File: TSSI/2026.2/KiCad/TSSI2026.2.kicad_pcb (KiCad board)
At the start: 2 copper layers, 66 x 35 mm, 32 parts, among them J1 Conn_01x02, J2 Conn_01x02, J3 Conn_02x02, Q1 IRLZ34N, T555 Test555, U1 LM555xN, U2 IRLZ34N, U3 IRLZ34N, U4 4001, U5 4069

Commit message: Add files via upload
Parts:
- moved U5 0.27 mm to (72.3, 24.5)

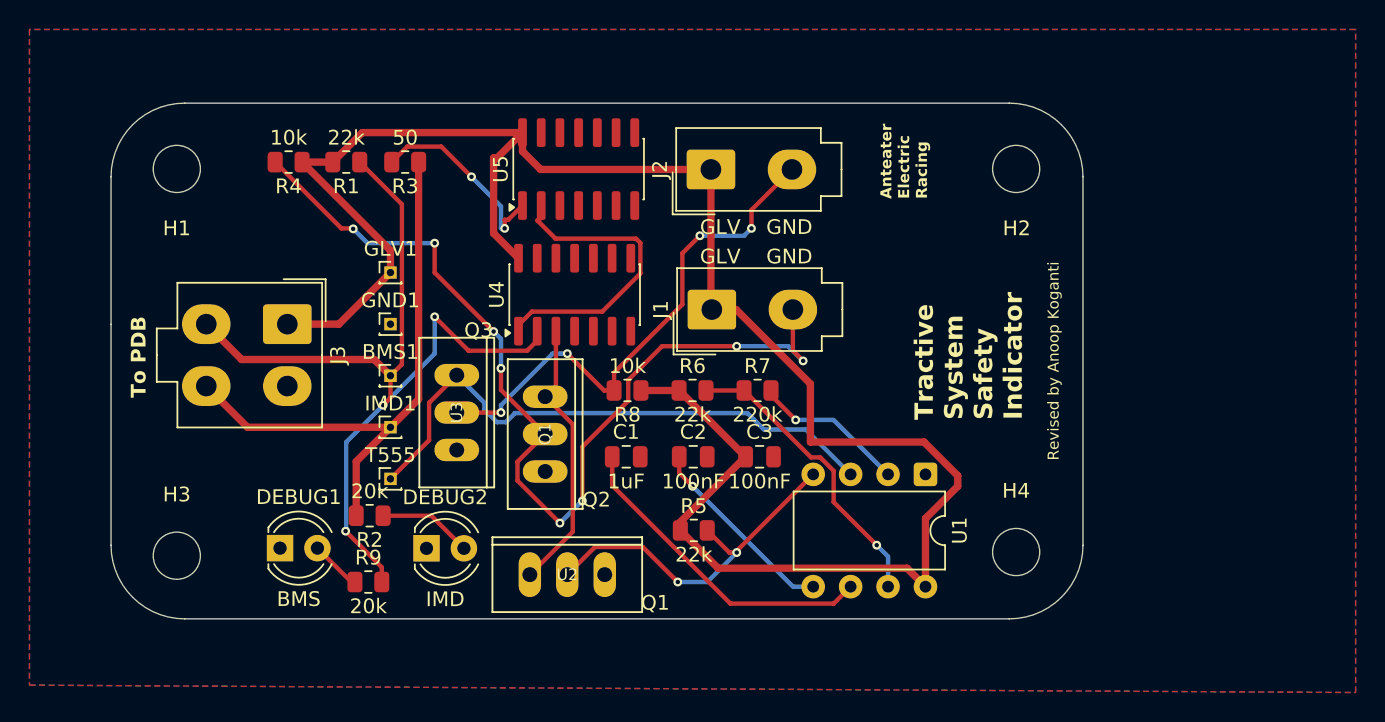
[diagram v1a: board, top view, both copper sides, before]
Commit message: Add silkscreen connectors
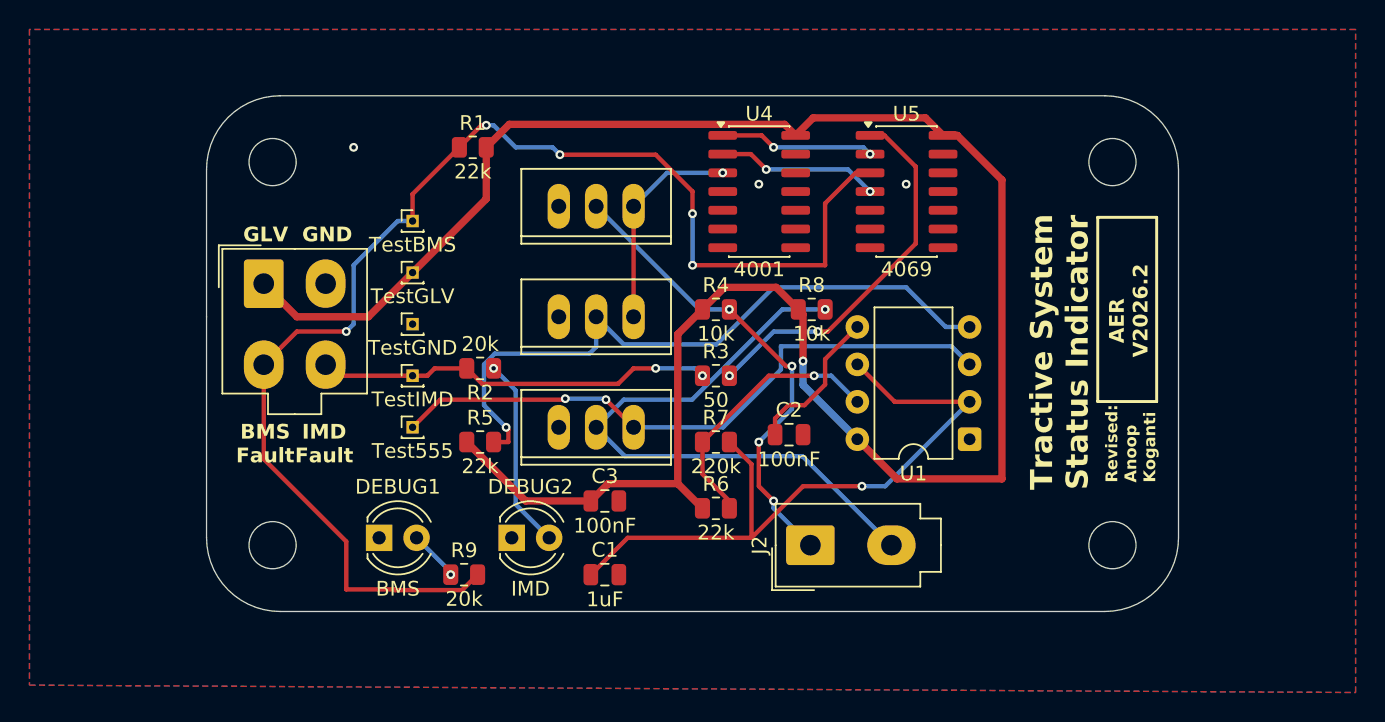
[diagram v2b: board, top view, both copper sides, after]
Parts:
- removed J1: Conn_01x02, Connector_Molex:Molex_Mini-Fit_Jr_5566-02A_2x01_P4.20mm_Vertical
- Q1, U2, U3: footprint IRLZ34N:TO-220_2_ -> Anteater-Electric-Racing electrical-pcbs main TSSI-2026.2_KiCad_Parts_IRLZ34N:TO-220_2_
- moved H3 63.5 mm to (108.5, 50.0)
- moved H2 56.6 mm to (51.5, 50.0)
- moved R4 30.7 mm to (81.6, 34.0), turned to 0 degrees
- moved H4 27.3 mm to (108.5, 24.0)
- moved J2 26.4 mm to (88.0, 50.0)
- moved R3 25.6 mm to (81.6, 38.5), turned to 0 degrees
- moved U5 22.3 mm to (94.5, 26.0), turned to 0 degrees
- moved U2 17.6 mm to (73.5, 34.5), turned to 180 degrees
- moved Q1 15.8 mm to (73.5, 27.0), turned to 180 degrees
- moved R5 15.7 mm to (65.6, 43.0)
- moved U4 14.3 mm to (84.5, 26.0), turned to 0 degrees
- moved R8 13.7 mm to (88.1, 34.0), turned to 0 degrees
- moved R2 12.5 mm to (65.6, 38.0)
- moved C3 10.9 mm to (74.0, 47.0)
- moved BMS1 10.6 mm to (61.0, 28.0)
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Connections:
- J2 pad 1: GLV -> Net-(J2-Pin_1)
- Q1 pad GND: Net-(J1-Pin_2) -> Net-(J2-Pin_1)
- R4 pad 2: Net-(J1-Pin_2) -> Net-(J2-Pin_1)
- U4 pad 2: BMS_FAULT -> Net-(U4-Pad2)
- U5 pad 3: (no net) -> BMS_FAULT
- U5 pad 4: (no net) -> Net-(U4-Pad2)
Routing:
- net Net-(J1-Pin_2): track 65.9 -> 0.00 mm, vias 8 -> 0
- net Net-(J2-Pin_1): track 0.00 -> 32.3 mm, vias 0 -> 4
- net BMS_FAULT: track 62.5 -> 90.2 mm, vias 3 -> 5
- net Net-(U1-R): track 24.2 -> 45.9 mm, vias 2 -> 1
- net Net-(U1-THR): track 32.4 -> 46.4 mm
- net IMD_FAULT: track 39.4 -> 27.2 mm, vias 0 -> 2
- net Net-(R3-Pad2): track 13.5 -> 25.6 mm
- net Net-(U4-Pad2): track 0.00 -> 11.1 mm, vias 0 -> 2
- net Net-(U4-Pad1): track 21.0 -> 10.5 mm, vias 0 -> 2
- net GLV: track 134.6 -> 141.8 mm, vias 0 -> 1
- net Net-(J2-Pin_2): track 35.4 -> 42.2 mm, vias 4 -> 1
- net Net-(DEBUG2-A): track 6.40 -> 13.1 mm, vias 0 -> 1
- net Net-(Q1-PadIN): track 18.8 -> 14.5 mm, vias 0 -> 1
- net Net-(T555-Pin_1): track 39.2 -> 43.1 mm, vias 0 -> 2
- net Net-(U1-CV): track 13.4 -> 10.3 mm, vias 1 -> 0
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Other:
- board text added: "AER V2026.2"
- board text added: "BMS Fault"
- board text added: "IMD Fault"
- board text added: "Revised: Anoop Koganti"
- board text added: "Tractive System Status Indicator"
- board text removed: "Anteater Electric Racing"
- board text removed: "Q1"
- board text removed: "Q2"
- board text removed: "Q3"
- board text removed: "Revised by Anoop Koganti"
- board text removed: "To PDB"
- board text removed: "Tractive System Safety Indicator"

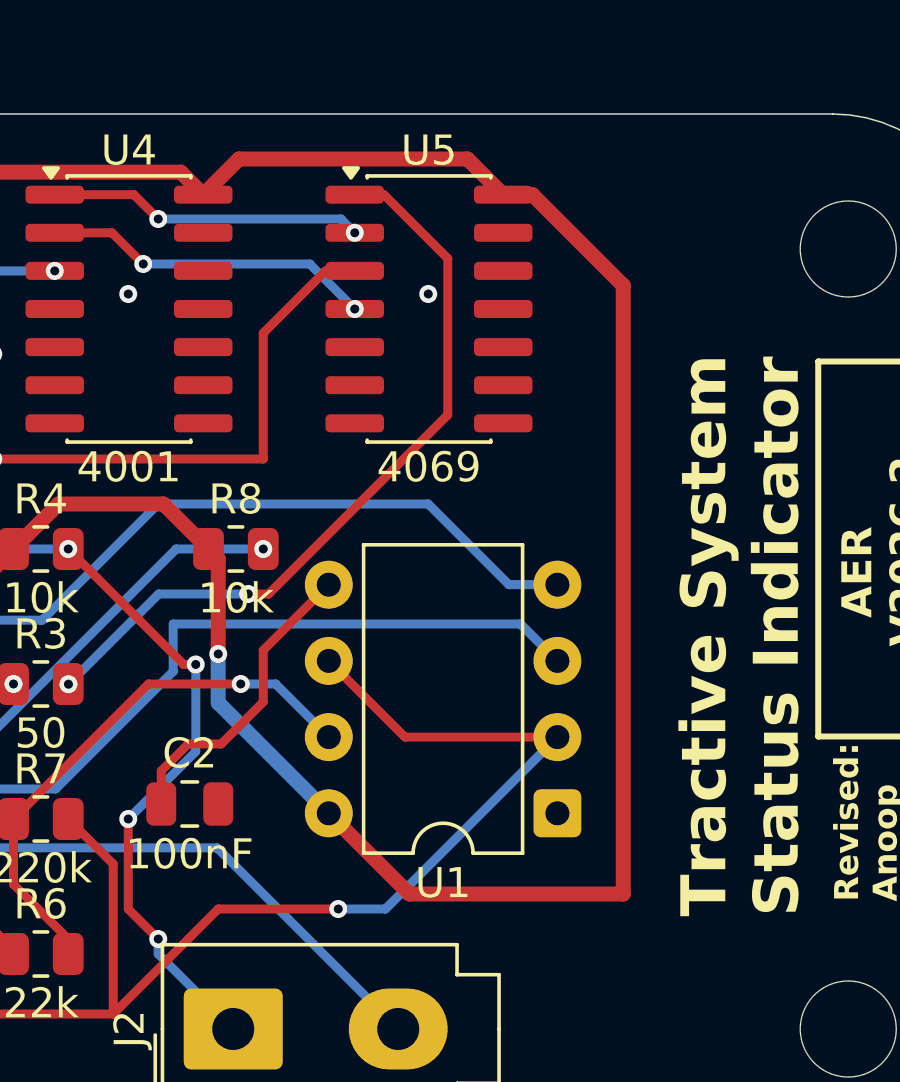
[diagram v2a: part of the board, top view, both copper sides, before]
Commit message: connected remaining pins to gnd
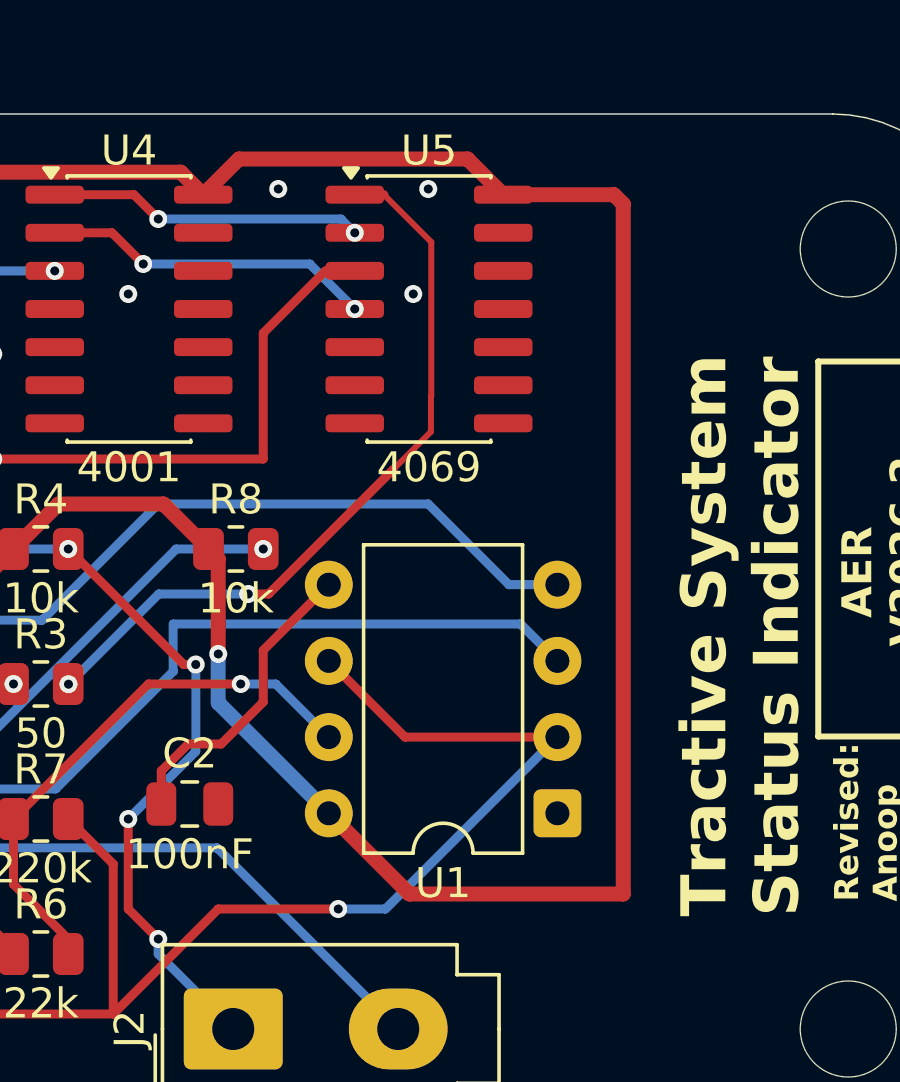
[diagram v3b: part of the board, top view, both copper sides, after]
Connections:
- net Net-(J2-Pin_1) renamed GREEN_LED
- net Net-(J2-Pin_2) renamed RED_LED
- U4 pad 10: (no net) -> unconnected-(U4-Pad10)
- U4 pad 11: (no net) -> unconnected-(U4-Pad11)
- U4 pad 12: (no net) -> GND
- U4 pad 13: (no net) -> GND
- U4 pad 4: (no net) -> unconnected-(U4-Pad4)
- U4 pad 5: (no net) -> GND
- U4 pad 6: (no net) -> GND
- U4 pad 8: (no net) -> GND
- U4 pad 9: (no net) -> GND
- U5 pad 10: (no net) -> unconnected-(U5-Pad10)
- U5 pad 11: (no net) -> GND
- U5 pad 12: (no net) -> unconnected-(U5-Pad12)
- U5 pad 13: (no net) -> GND
- U5 pad 5: (no net) -> GND
- U5 pad 6: (no net) -> unconnected-(U5-Pad6)
- U5 pad 8: (no net) -> unconnected-(U5-Pad8)
- U5 pad 9: (no net) -> GND
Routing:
- net GLV: track 141.8 -> 143.4 mm
- net GND: vias 3 -> 5
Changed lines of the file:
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@@
 	(net 4 "GLV")
 	(net 5 "IMD_FAULT")
-	(net 6 "Net-(J2-Pin_1)")
-	(net 7 "Net-(J2-Pin_2)")
+	(net 6 "GREEN_LED")
+	(net 7 "RED_LED")
 	(net 8 "Net-(DEBUG1-A)")
 	(net 9 "Net-(U1-DIS)")
@@
 	(net 16 "Net-(U4-Pad1)")
 	(net 17 "Net-(U4-Pad2)")
+	(net 18 "unconnected-(U4-Pad11)")
+	(net 19 "unconnected-(U4-Pad10)")
+	(net 20 "unconnected-(U4-Pad4)")
+	(net 21 "unconnected-(U5-Pad10)")
+	(net 22 "unconnected-(U5-Pad6)")
+	(net 23 "unconnected-(U5-Pad12)")
+	(net 24 "unconnected-(U5-Pad8)")
 	(footprint "LED_THT:LED_D4.0mm"
 		(layer "F.Cu")
@@
 			(layers "*.Cu" "*.Mask")
 			(remove_unused_layers no)
-			(net 7 "Net-(J2-Pin_2)")
+			(net 7 "RED_LED")
 			(pintype "passive")
 			(solder_mask_margin 0.102)
@@
 			(remove_unused_layers no)
 			(roundrect_rratio 0.092593)
-			(net 6 "Net-(J2-Pin_1)")
+			(net 6 "GREEN_LED")
 			(pinfunction "Pin_1")
 			(pintype "passive")
@@
 			(layers "*.Cu" "*.Mask")
 			(remove_unused_layers no)
-			(net 7 "Net-(J2-Pin_2)")
+			(net 7 "RED_LED")
 			(pinfunction "Pin_2")
 			(pintype "passive")
@@
 			(layers "F.Cu" "F.Mask" "F.Paste")
 			(roundrect_rratio 0.25)
+			(net 11 "GND")
+			(pintype "input")
 		)
 		(pad "6" smd roundrect
@@
 			(layers "F.Cu" "F.Mask" "F.Paste")
 			(roundrect_rratio 0.25)
+			(net 22 "unconnected-(U5-Pad6)")
+			(pintype "output+no_connect")
 		)
 		(pad "7" smd roundrect
@@
 			(layers "F.Cu" "F.Mask" "F.Paste")
 			(roundrect_rratio 0.25)
+			(net 24 "unconnected-(U5-Pad8)")
+			(pintype "output+no_connect")
 		)
 		(pad "9" smd roundrect
@@
 			(layers "F.Cu" "F.Mask" "F.Paste")
 			(roundrect_rratio 0.25)
+			(net 11 "GND")
+			(pintype "input")
 		)
 		(pad "10" smd roundrect
@@
 			(layers "F.Cu" "F.Mask" "F.Paste")
 			(roundrect_rratio 0.25)
+			(net 21 "unconnected-(U5-Pad10)")
+			(pintype "output+no_connect")
 		)
 		(pad "11" smd roundrect
@@
 			(layers "F.Cu" "F.Mask" "F.Paste")
 			(roundrect_rratio 0.25)
+			(net 11 "GND")
+			(pintype "input")
 		)
 		(pad "12" smd roundrect
@@
 			(layers "F.Cu" "F.Mask" "F.Paste")
 			(roundrect_rratio 0.25)
+			(net 23 "unconnected-(U5-Pad12)")
+			(pintype "output+no_connect")
 		)
 		(pad "13" smd roundrect
@@
 			(layers "F.Cu" "F.Mask" "F.Paste")
 			(roundrect_rratio 0.25)
+			(net 11 "GND")
+			(pintype "input")
 		)
 		(pad "14" smd roundrect
@@
 			(layers "F.Cu" "F.Mask" "F.Paste")
 			(roundrect_rratio 0.25)
+			(net 20 "unconnected-(U4-Pad4)")
+			(pintype "output+no_connect")
 		)
 		(pad "5" smd roundrect
@@
 			(layers "F.Cu" "F.Mask" "F.Paste")
 			(roundrect_rratio 0.25)
+			(net 11 "GND")
+			(pintype "input")
 		)
 		(pad "6" smd roundrect
@@
 			(layers "F.Cu" "F.Mask" "F.Paste")
 			(roundrect_rratio 0.25)
+			(net 11 "GND")
+			(pintype "input")
 		)
 		(pad "7" smd roundrect
@@
 			(layers "F.Cu" "F.Mask" "F.Paste")
 			(roundrect_rratio 0.25)
+			(net 11 "GND")
+			(pintype "input")
 		)
 		(pad "9" smd roundrect
@@
 			(layers "F.Cu" "F.Mask" "F.Paste")
 			(roundrect_rratio 0.25)
+			(net 11 "GND")
+			(pintype "input")
 		)
 		(pad "10" smd roundrect
@@
 			(layers "F.Cu" "F.Mask" "F.Paste")
 			(roundrect_rratio 0.25)
+			(net 19 "unconnected-(U4-Pad10)")
+			(pintype "output+no_connect")
 		)
 		(pad "11" smd roundrect
@@
 			(layers "F.Cu" "F.Mask" "F.Paste")
 			(roundrect_rratio 0.25)
+			(net 18 "unconnected-(U4-Pad11)")
+			(pintype "output+no_connect")
 		)
 		(pad "12" smd roundrect
@@
 			(layers "F.Cu" "F.Mask" "F.Paste")
 			(roundrect_rratio 0.25)
+			(net 11 "GND")
+			(pintype "input")
 		)
 		(pad "13" smd roundrect
@@
 			(layers "F.Cu" "F.Mask" "F.Paste")
 			(roundrect_rratio 0.25)
+			(net 11 "GND")
+			(pintype "input")
 		)
 		(pad "14" smd roundrect
@@
 			(layers "*.Cu" "*.Mask")
 			(remove_unused_layers no)
-			(net 6 "Net-(J2-Pin_1)")
+			(net 6 "GREEN_LED")
 			(pintype "passive")
 			(solder_mask_margin 0.102)
@@
 			(layers "F.Cu" "F.Mask" "F.Paste")
 			(roundrect_rratio 0.243902)
-			(net 6 "Net-(J2-Pin_1)")
+			(net 6 "GREEN_LED")
 			(pintype "passive")
 		)
@@
 			(layers "F.Cu" "F.Mask" "F.Paste")
 			(roundrect_rratio 0.243902)
-			(net 7 "Net-(J2-Pin_2)")
+			(net 7 "RED_LED")
 			(pintype "passive")
 		)
@@
 	)
 	(segment
-		(start 101 25.215001)
-		(end 101 45.5)
+		(start 100.69 22.19)
+		(end 101 22.5)
 		(width 0.5)
 		(layer "F.Cu")
@@
 	)
 	(segment
-		(start 101 45.5)
-		(end 93.875 45.5)
+		(start 86.249 21.439)
+		(end 87 22.19)
 		(width 0.5)
 		(layer "F.Cu")
@@
 	)
 	(segment
-		(start 86.249 21.439)
-		(end 87 22.19)
+		(start 93.875 45.5)
+		(end 91.185 42.81)
 		(width 0.5)
 		(layer "F.Cu")
@@
 	)
 	(segment
+		(start 97 22.19)
+		(end 100.69 22.19)
+		(width 0.5)
+		(layer "F.Cu")
+		(net 4)
+	)
+	(segment
 		(start 50.9 32.25)
 		(end 53.15 34.5)
@@
 	)
 	(segment
-		(start 97 22.19)
-		(end 97.974999 22.19)
-		(width 0.5)
-		(layer "F.Cu")
-		(net 4)
-	)
-	(segment
 		(start 87 22.19)
 		(end 88.19 21)
@@
 	)
 	(segment
-		(start 88.19 21)
-		(end 95.81 21)
+		(start 101 45.5)
+		(end 93.875 45.5)
 		(width 0.5)
 		(layer "F.Cu")
@@
 	)
 	(segment
-		(start 93.875 45.5)
-		(end 91.185 42.81)
+		(start 88.19 21)
+		(end 95.81 21)
 		(width 0.5)
 		(layer "F.Cu")
@@
 	)
 	(segment
+		(start 101 22.5)
+		(end 101 45.5)
+		(width 0.5)
+		(layer "F.Cu")
+		(net 4)
+	)
+	(segment
 		(start 68.675 47)
 		(end 64.675 43)
@@
 	)
 	(segment
-		(start 97.974999 22.19)
-		(end 101 25.215001)
-		(width 0.5)
-		(layer "F.Cu")
-		(net 4)
-	)
-	(segment
 		(start 87.5 34.325)
 		(end 87.175 34)
@@
 	)
 	(via
-		(at 94.5 25.5)
+		(at 94 25.5)
 		(size 0.6)
 		(drill 0.3)
@@
 		(net 11)
 	)
+	(via
+		(at 89.5 22)
+		(size 0.6)
+		(drill 0.3)
+		(layers "F.Cu" "B.Cu")
+		(free yes)
+		(net 11)
+	)
+	(via
+		(at 94.5 22)
+		(size 0.6)
+		(drill 0.3)
+		(layers "F.Cu" "B.Cu")
+		(free yes)
+		(net 11)
+	)
 	(segment
 		(start 93.340347 31.340347)
@@
 	)
 	(segment
-		(start 93.024999 22.19)
-		(end 95.151 24.316001)
-		(width 0.3)
+		(start 93.340347 31.340347)
+		(end 94.590347 30.090347)
+		(width 0.2)
+		(layer "F.Cu")
+		(net 12)
+	)
+	(segment
+		(start 94.590347 28.909653)
+		(end 94.601 28.899)
+		(width 0.2)
 		(layer "F.Cu")
 		(net 12)
@@
 	)
 	(segment
-		(start 95.151 24.316001)
-		(end 95.151 29.529695)
-		(width 0.3)
+		(start 93.024999 22.19)
+		(end 94.601 23.766001)
+		(width 0.2)
 		(layer "F.Cu")
 		(net 12)
 	)
 	(segment
-		(start 95.151 29.529695)
-		(end 93.340347 31.340347)
-		(width 0.3)
+		(start 94.590347 30.090347)
+		(end 94.590347 28.909653)
+		(width 0.2)
 		(layer "F.Cu")
 		(net 12)
@@
 		(layer "F.Cu")
 		(net 12)
+	)
+	(segment
+		(start 94.601 23.766001)
+		(end 94.601 28.899)
+		(width 0.2)
+		(layer "F.Cu")
+		(net 12)
